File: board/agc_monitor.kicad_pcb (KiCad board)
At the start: 4 copper layers, 132.5 x 73 mm, 70 parts, among them J1 Conn_01x03, J2 Conn_01x03, J3 Conn_01x08, J4 Styx_P4, J5 Styx_P5, P1 test_connector, Q1 MMBT3904, Q2 MMBT3904, Q3 MMBT3904, Q4 MMBT3904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

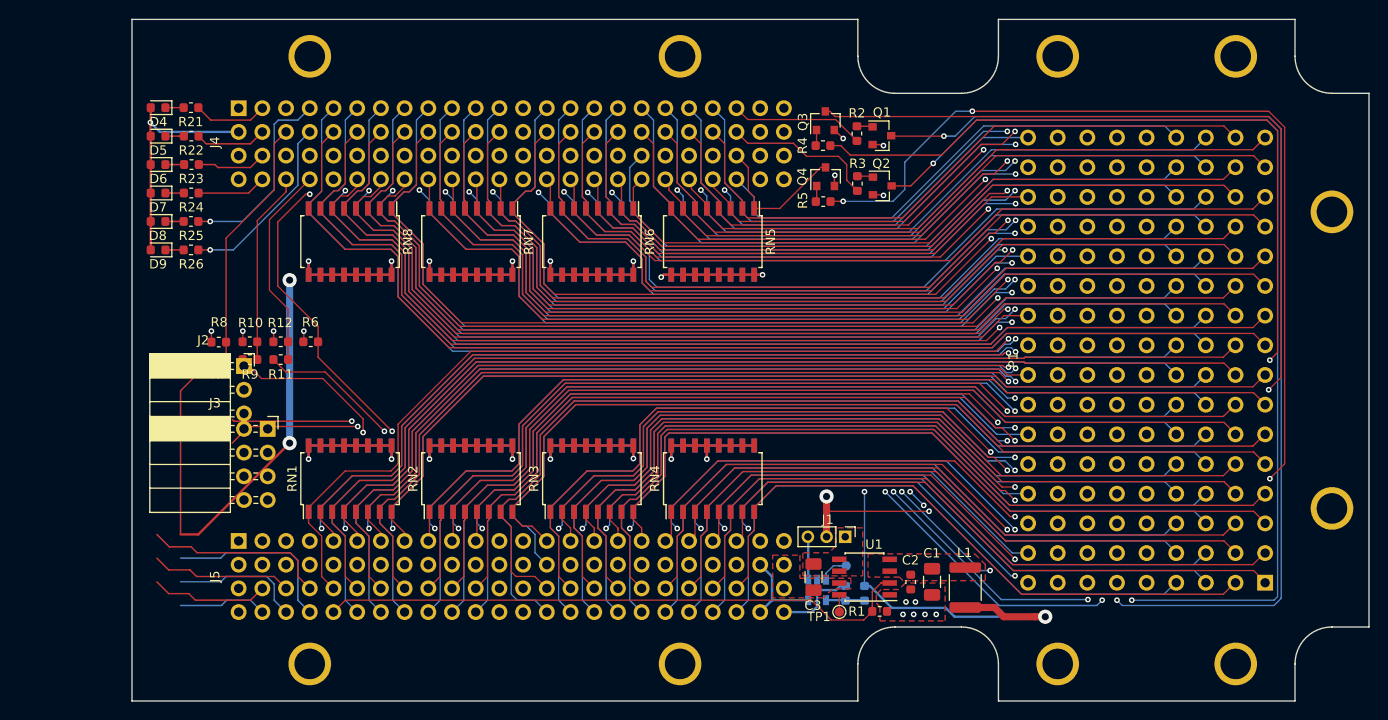
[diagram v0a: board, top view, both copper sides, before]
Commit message: Board: more rearranging work on the front; a bit more yet to come
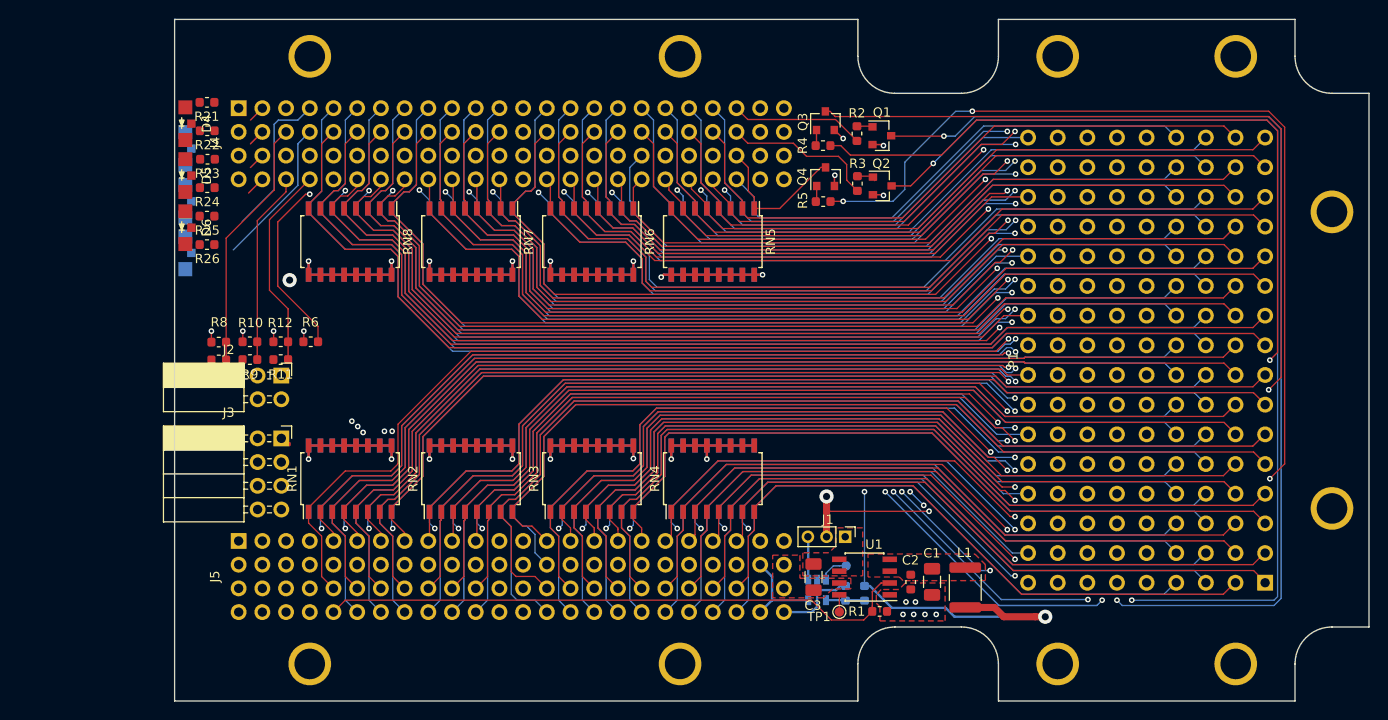
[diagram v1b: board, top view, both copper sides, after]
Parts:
- D4, D5, D6: value LED -> LED_PAD; footprint LED_SMD:LED_0603_1608Metric -> agc_monitor:apa3010
- D7, D8, D9: value LED -> LED_PAD; footprint LED_SMD:LED_0603_1608Metric -> agc_monitor:apa3010; moved to B.Cu
- J2: value Conn_01x03 -> Conn_01x04; footprint Connector_PinSocket_2.54mm:PinSocket_1x03_P2.54mm_Horizontal -> Connector_PinSocket_2.54mm:PinSocket_2x02_P2.54mm_Horizontal
- moved D6 7.37 mm to (100.2, 87.4), turned to 90 degrees
- moved D7 5.59 mm to (100.2, 78.9), turned to 270 degrees
- moved D5 5.14 mm to (100.2, 81.8), turned to 90 degrees
- moved J2 4.13 mm to (110.5, 103.3)
- moved D8 3.63 mm to (100.2, 84.6), turned to 270 degrees
- moved D4 3.39 mm to (100.2, 76.3), turned to 90 degrees
- moved D9 2.94 mm to (100.2, 90.1), turned to 270 degrees
- moved R21 1.81 mm to (102.5, 74.0)
- moved R22 1.81 mm to (102.6, 77.0)
- moved R23 1.81 mm to (102.6, 80.1)
- moved R24 1.81 mm to (102.6, 83.1)
- moved R25 1.81 mm to (102.5, 86.2)
- moved R26 1.81 mm to (102.5, 89.2)
- moved J3 1.78 mm to (110.5, 110.0)
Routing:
- net +3V3_IO: track 397.0 -> 341.3 mm, vias 20 -> 19
- net /StyxConnectors/3V3_LED: track 25.2 -> 0.00 mm, vias 1 -> 0
- net /StyxConnectors/DBG1: track 19.8 -> 0.00 mm
- net /StyxConnectors/DBG2: track 19.2 -> 0.00 mm
- net +4SW: track 121.9 -> 104.9 mm
- net /StyxConnectors/DBG3: track 15.2 -> 0.00 mm
- net BPLSSW: track 93.9 -> 78.9 mm
- net CTRL2: track 107.8 -> 93.6 mm
- net /StyxConnectors/DBG4: track 14.1 -> 0.00 mm
- net CTRL1: track 101.8 -> 88.9 mm
- net MTLO: track 113.7 -> 100.8 mm
- net /StyxConnectors/DBG5: track 12.6 -> 0.00 mm
- net /StyxConnectors/DBG6: track 9.53 -> 0.00 mm
- net /StyxConnectors/LED1: track 7.94 -> 1.81 mm
- net /StyxConnectors/LED2: track 7.70 -> 1.81 mm
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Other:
- board size 132.5 x 73 mm -> 128 x 73 mm

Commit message: Board: Reshaped and relocated some components; board may extend soon to allow a cover to neck in
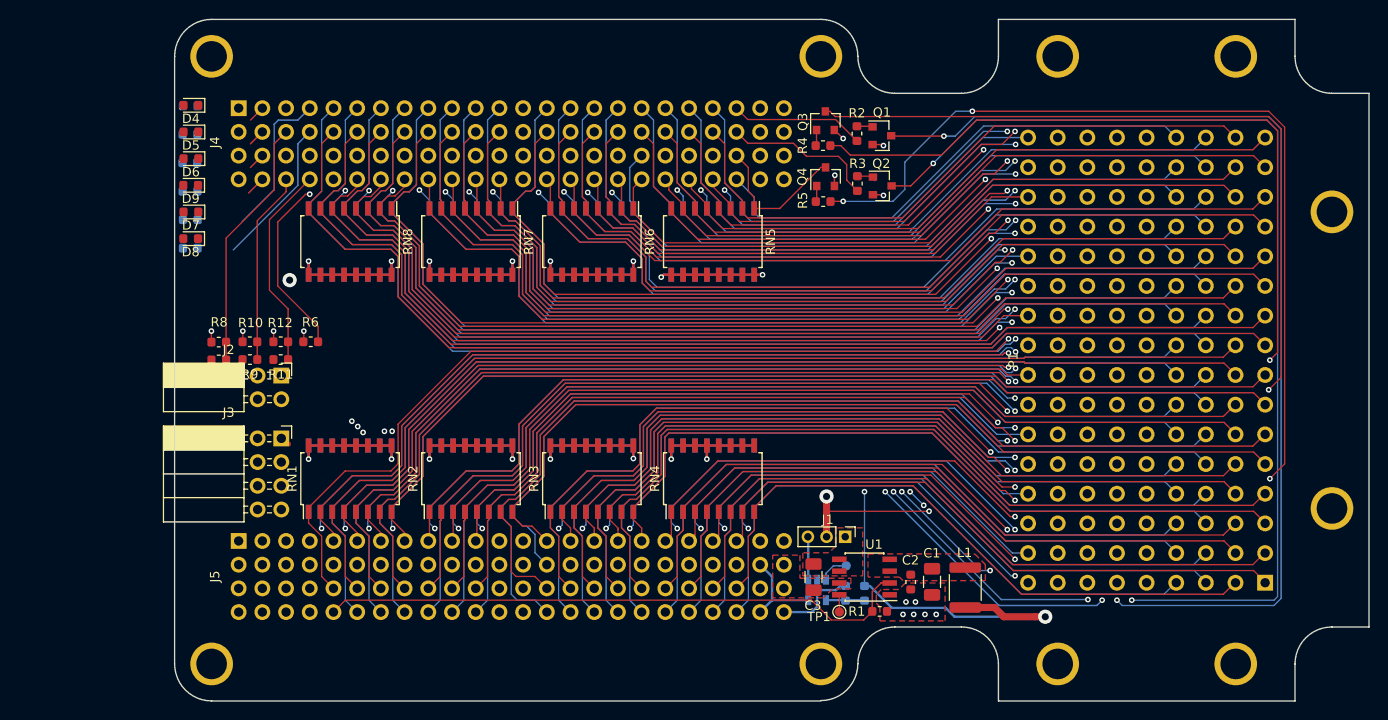
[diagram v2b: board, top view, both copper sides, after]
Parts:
- D4, D5, D6: value LED_PAD -> LED; footprint agc_monitor:apa3010 -> LED_SMD:LED_0603_1608Metric
- D7, D8, D9: value LED_PAD -> LED; footprint agc_monitor:apa3010 -> LED_SMD:LED_0603_1608Metric; moved to F.Cu
- R21, R22, R23, R24, R25, R26: moved to B.Cu
- moved H10 15.1 mm to (168.3, 69.0)
- moved H9 15.1 mm to (168.3, 134.2)
- moved H7 10.5 mm to (103.0, 134.2)
- moved H8 10.5 mm to (103.0, 69.0)
- moved D6 7.43 mm to (100.8, 80.0), turned to 180 degrees
- moved D9 7.26 mm to (100.8, 82.9), turned to 180 degrees
- moved D7 6.82 mm to (100.8, 85.7), turned to 180 degrees
- moved D5 4.71 mm to (100.8, 77.2), turned to 180 degrees
- moved D8 4.04 mm to (100.8, 88.6), turned to 180 degrees
- moved D4 2.06 mm to (100.8, 74.3), turned to 180 degrees
- moved R23 1.93 mm to (100.7, 80.5), turned to 180 degrees
- moved R22 1.88 mm to (100.7, 77.4), turned to 180 degrees
- moved R24 1.88 mm to (100.7, 83.5), turned to 180 degrees
- moved R21 1.83 mm to (100.7, 74.4), turned to 180 degrees
- moved R25 1.83 mm to (100.7, 86.6), turned to 180 degrees
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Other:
- outline, holes or cut-outs redrawn

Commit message: Board: finalized v1.1 (barring any last-minute tweaks)
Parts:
- removed D7, D8, D9: LED, LED_SMD:LED_0603_1608Metric
- removed H10, H7, H8, H9: MountingHole, agc_monitor:MountingHole_ANSI_4
- added D1: LED, LED_SMD:LED_0603_1608Metric, F.Cu at (84.1, 74.3)
- added D2: LED, LED_SMD:LED_0603_1608Metric, F.Cu at (84.1, 77.2)
- added D3: LED, LED_SMD:LED_0603_1608Metric, F.Cu at (84.1, 80.0)
- R21, R22, R23, R24, R25, R26: moved to F.Cu
- moved H6 136.6 mm to (87.5, 134.2)
- moved H3 124.5 mm to (87.5, 69.0)
- moved H5 56.7 mm to (193.7, 134.2)
- moved H1 19.1 mm to (212.8, 69.0)
- moved H2 19.1 mm to (193.7, 69.0)
- moved D4 18.7 mm to (84.1, 82.9)
- moved D5 18.7 mm to (84.1, 85.7)
- moved D6 18.7 mm to (84.1, 88.6)
- moved R26 13.1 mm to (87.7, 88.6), turned to 0 degrees
- moved R25 13.1 mm to (87.7, 85.7), turned to 0 degrees
- moved R21 13.0 mm to (87.7, 74.3), turned to 0 degrees
- moved R23 13.0 mm to (87.7, 80.0), turned to 0 degrees
- moved R22 13.0 mm to (87.7, 77.2), turned to 0 degrees
- moved R24 13.0 mm to (87.7, 82.9), turned to 0 degrees
- moved Q4 12.0 mm to (156.8, 81.9)
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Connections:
- J2 pad 2: CTRL2 -> GND
- J2 pad 3: GND -> CTRL2
- J5 pad 11: /StyxConnectors/DBG3 -> /StyxConnectors/DBG6
- J5 pad 12: /StyxConnectors/DBG4 -> /StyxConnectors/DBG1
- J5 pad 15: /StyxConnectors/DBG1 -> /StyxConnectors/DBG2
- J5 pad 16: /StyxConnectors/DBG2 -> /StyxConnectors/DBG4
- J5 pad 7: /StyxConnectors/DBG5 -> /StyxConnectors/DBG3
- J5 pad 8: /StyxConnectors/DBG6 -> /StyxConnectors/DBG5
- R21 pad 1: Net-(D4-Pad1) -> Net-(D1-Pad1)
- R22 pad 1: Net-(D5-Pad1) -> Net-(D2-Pad1)
- R23 pad 1: Net-(D6-Pad1) -> Net-(D3-Pad1)
- R24 pad 1: Net-(D7-Pad1) -> Net-(D4-Pad1)
- R25 pad 1: Net-(D8-Pad1) -> Net-(D5-Pad1)
- R26 pad 1: Net-(D9-Pad1) -> Net-(D6-Pad1)
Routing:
- net +3V3_IO: track 341.3 -> 383.5 mm, vias 19 -> 20
- net +4SW: track 104.9 -> 145.9 mm
- net BPLSSW: track 78.9 -> 106.0 mm
- net /StyxConnectors/3V3_LED: track 0.00 -> 25.5 mm
- net MTLO: track 100.8 -> 126.2 mm
- net NHALGA: track 194.5 -> 218.5 mm
- net CTRL1: track 88.9 -> 110.1 mm
- net CTRL2: track 93.6 -> 114.7 mm
- net /StyxConnectors/DBG1: track 0.00 -> 19.7 mm
- net /StyxConnectors/DBG3: track 0.00 -> 14.7 mm
- net /StyxConnectors/DBG5: track 0.00 -> 14.7 mm
- net /StyxConnectors/DBG2: track 0.00 -> 14.6 mm
- net /StyxConnectors/DBG4: track 0.00 -> 14.6 mm
- net STRT1: track 113.5 -> 125.5 mm
- net MSQ14: track 71.3 -> 83.3 mm
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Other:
- board size 128 x 73 mm -> 144.6 x 73 mm
- board text added: "01"
- board text added: "02"
- board text added: "03"
- board text added: "04"
- board text added: "05"
- board text added: "06"
- board text added: "07"
- board text added: "08"
- board text added: "09"
- board text added: "1"
- board text added: "10"
- board text added: "11"
- board text added: "12"
- board text added: "13"
- board text added: "14"
- board text added: "15"
- board text added: "16"
- board text added: "2"
- board text added: "3"
- board text added: "4"
- board text added: "5"
- board text added: "6"
- board text added: "7"
- board text added: "8"
- board text added: "9"
- board text added: "A52"
- board text added: "AGC Monitor v1.1 Mike Stewart"
- board text added: "CTRL"
- board text added: "V 2 4 6 1 3 5 G"
